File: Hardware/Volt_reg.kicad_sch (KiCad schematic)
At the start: 0 parts

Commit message: USB-C + Voltage stuff
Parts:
- added C28, C29, C30, C33: 0.1uF, Capacitor_SMD:C_0402_1005Metric, symbol Device:C_Small
- added C31: 1uF, Capacitor_SMD:C_0402_1005Metric, symbol Device:C_Small
- added C32: 0.1uF, Capacitor_SMD:C_0603_1608Metric, symbol Device:C_Small
- added D7: P6SMBJ28CA, Diode_SMD:D_SMA, symbol Device:D_TVS_Small_Filled
- added Q2, Q3: BSZ025N04LS, iclr:BSZ025N04LS, symbol iclr:BSZ025N04LS
- added R26: 2m, Resistor_SMD:R_2512_6332Metric_Pad1.40x3.35mm_HandSolder, symbol Device:R
- added R27, R28: 10, Resistor_SMD:R_0402_1005Metric, symbol Device:R_Small
- added R29, R30: 3.3k, Resistor_SMD:R_0402_1005Metric, symbol Device:R_Small
- added R31: 10k, Resistor_SMD:R_0402_1005Metric, symbol Device:R_Small
- added R32: 100k, Resistor_SMD:R_0402_1005Metric, symbol Device:R_Small
- added R33: 5.1k, Resistor_SMD:R_0402_1005Metric, symbol Device:R_Small
- added R34: 4.22k, Resistor_SMD:R_0402_1005Metric, symbol Device:R_Small
- added TP11, TP12: TestPoint, TestPoint:TestPoint_Pad_D1.0mm, symbol Connector:TestPoint
- added U8: INA219AxDCN, Package_TO_SOT_SMD:SOT-23-8, symbol Sensor_Energy:INA219AxDCN
- added U9: LM74810, iclr:SON50P300X300X80-13N-D, symbol iclr:LM74810QDRRRQ1
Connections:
- new net: R33.1, R34.2, U9.5 (OV)
- new net: R32.1, U9.4 (SW)
- new net +3V3: C29.1, R29.1, R30.1, U8.4 (VS)
- new net BUS_VMON: R32.2, R33.2
- new net C: C31.1, C32.1, Q2.5 (D), Q2.6 (D), Q2.7 (D), Q2.8 (D), Q2.A5 (D), Q3.5 (D), Q3.6 (D), Q3.7 (D), Q3.8 (D), Q3.A5 (D), U9.10 (VS), U9.12 (C)
- new net CAP: C31.2, U9.11 (CAP)
- new net DGate: Q2.4 (G), U9.1 (DGATE)
- new net DeployV_Post_Diode: R26.1, R27.1
- new net EN: R31.1, U9.6 (EN/UVLO)
- new net GND: C29.2, C30.2, C32.2, C33.2, D7.2 (A2), R31.2, R34.1, U8.3 (GND), U8.7 (A0), U8.8 (A1), U9.7 (GND)
- new net HGate: Q3.4 (G), U9.8 (HGATE)
- new net PyroPWR: R26.2, R28.1
- new net SCL: R30.2, TP12.1, U8.5 (SCL)
- new net SDA-CurrentSens: R29.2, TP11.1, U8.6 (SDA)
- new net SHNT_IN+: C28.1, R27.2, U8.1 (IN+)
- new net SHNT_IN-: C28.2, C33.1, Q3.1 (S), Q3.2 (S), Q3.3 (S), Q3.A1 (S), R28.2, U8.2 (IN-), U9.9 (OUT)
- new net VIN: C30.1, D7.1 (A1), Q2.1 (S), Q2.2 (S), Q2.3 (S), Q2.A1 (S), U9.2 (A), U9.3 (VSNS)
- no-connect marks 0 -> 1
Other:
- note added: "Add 8A buck-boost converter, takes VIN outputs into High side switch. 8A: https://www.ti.com/lit/ds/symlink/tps55289.pdf?HQS=dis-mous-null-mousermode-dsf-pf-null-wwe&ts=1738081315650&ref_url=https%253A%252F%252Fwww.mouser.com%252F 16A: https://www.ti.com/lit/ds/slvsf01b/slvsf01b.pdf?ts=1734821027897&ref_url=https%253A%252F%252Fwww.google.com%252Furl%253Fq%253Dhttps%253A%252F%252Fwww.ti.com%252Fli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"
- note added: "Batt Mon - 3.0V out @ 35V in Overvoltage cutoff - 32V Check sizing script"

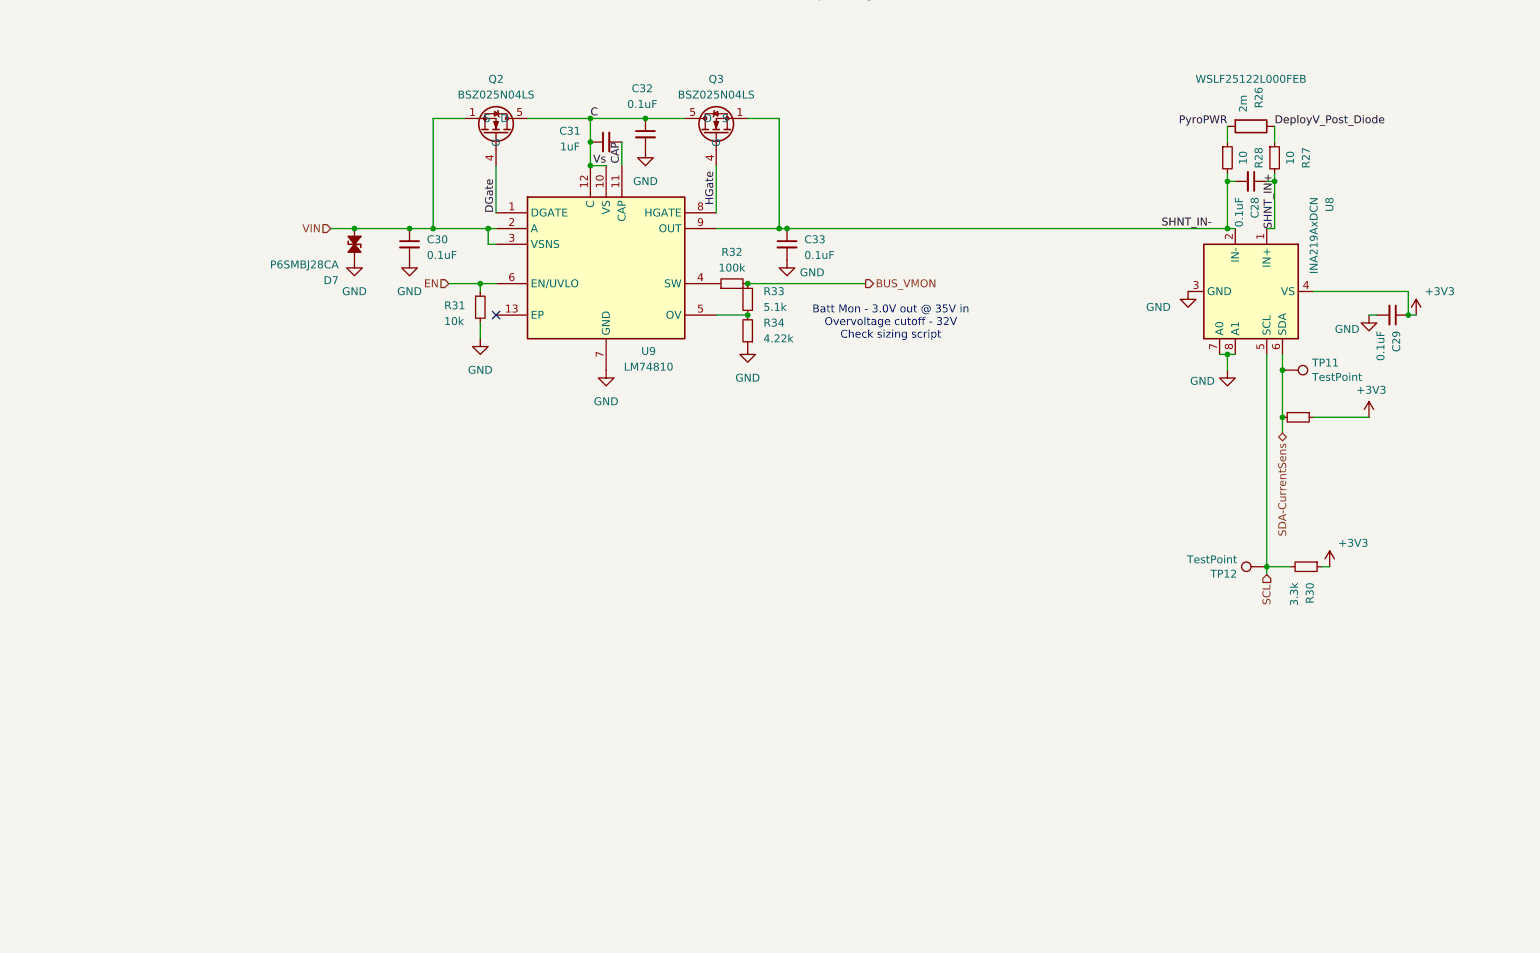
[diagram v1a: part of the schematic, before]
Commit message: Voltage regulation done + used photo ic sensor library
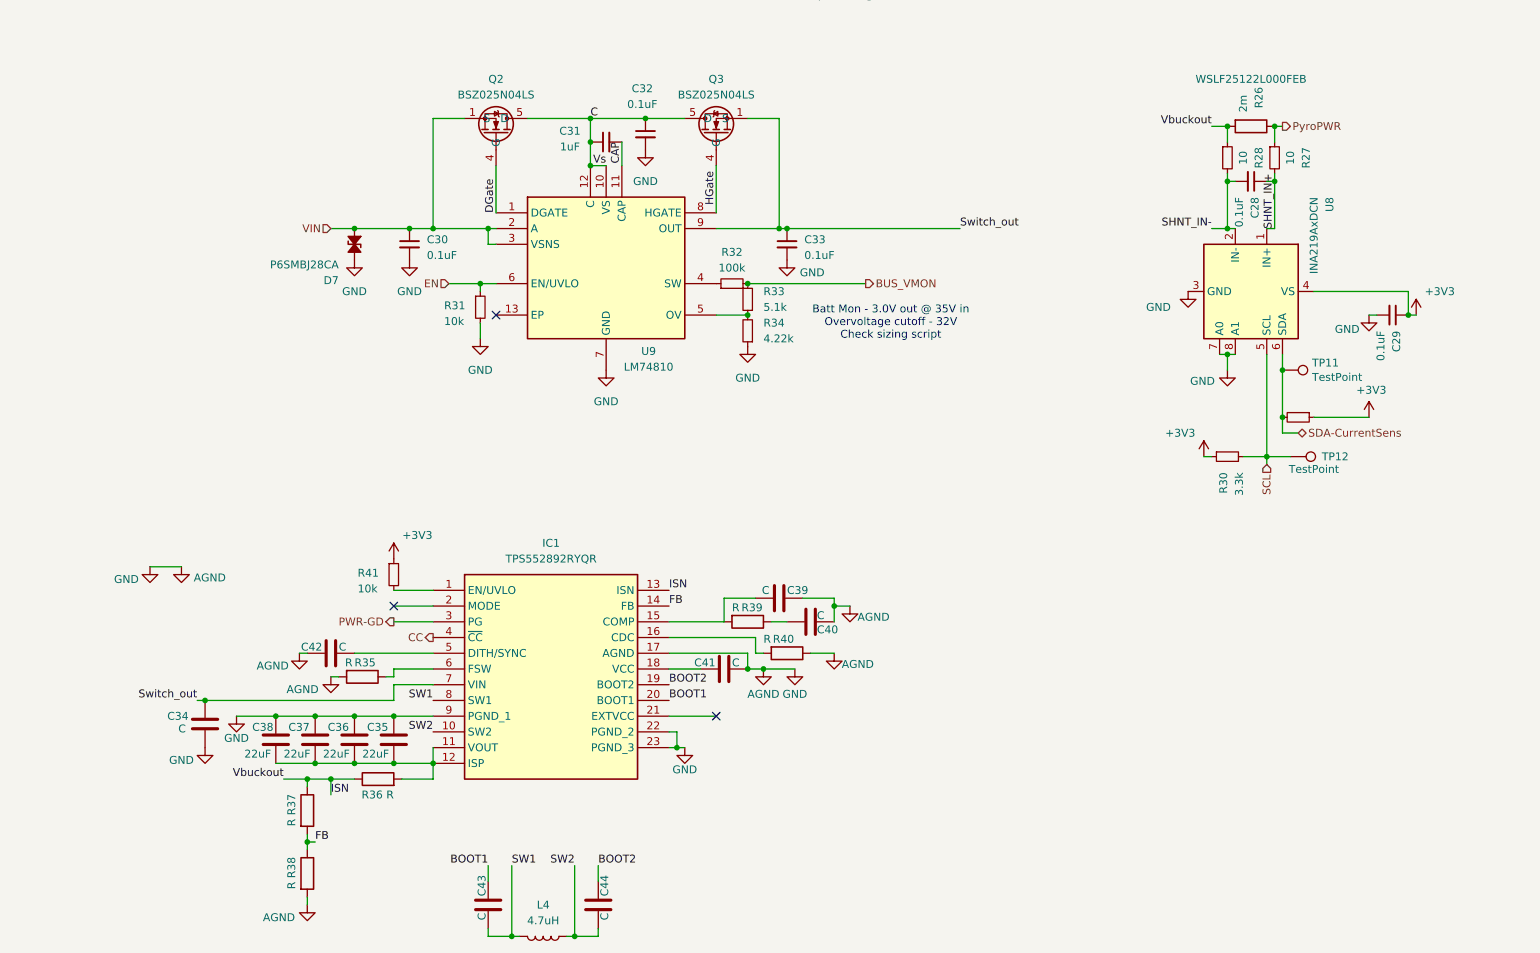
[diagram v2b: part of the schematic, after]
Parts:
- added C34, C39, C40, C41, C42, C43, C44: C, symbol Device:C
- added C35, C36, C37, C38: 22uF, symbol Device:C
- added IC1: TPS552892RYQR, TPS552892RYQR, symbol iclr:TPS552892RYQR
- added L4: 4.7uH, symbol Device:L
- added R35, R36, R37, R38, R39, R40: R, symbol Device:R
- added R41: 10k, Resistor_SMD:R_0402_1005Metric, symbol Device:R_Small
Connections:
- net DeployV_Post_Diode is gone; now on net PyroPWR: R26.1, R27.1
- net +3V3: now also R41.1
- net PyroPWR: no longer R26.2, R28.1
- net SHNT_IN-: no longer C33.1, Q3.1 (S), Q3.2 (S), Q3.3 (S), Q3.A1 (S), U9.9 (OUT)
- net GND renamed AGND
- net AGND: now also C34.2, C35.1, C36.1, C37.1, C38.1, C39.1, C40.1, C41.1, C42.2, IC1.17 (AGND), IC1.22 (PGND_2), IC1.23 (PGND_3), IC1.9 (PGND_1), R35.2, R38.2, R40.1
- new net: IC1.6 (FSW), R35.1
- new net: C42.1, IC1.5 (DITH/SYNC)
- new net: C35.2, C36.2, C37.2, C38.2, IC1.11 (VOUT), IC1.12 (ISP), R36.2
- new net: IC1.16 (CDC), R40.2
- new net: C40.2, R39.1
- new net: C39.2, IC1.15 (COMP), R39.2
- new net: IC1.1 (EN/UVLO), R41.2
- new net: C41.2, IC1.18 (VCC)
- new net BOOT1: C43.2, IC1.20 (BOOT1)
- new net BOOT2: C44.2, IC1.19 (BOOT2)
- new net CC: IC1.4 (~{CC})
- new net FB: IC1.14 (FB), R37.2, R38.1
- new net ISN: IC1.13 (ISN), R26.2, R28.1, R36.1, R37.1
- new net PWR-GD: IC1.3 (PG)
- new net SW1: C43.1, IC1.8 (SW1), L4.2
- new net SW2: C44.1, IC1.10 (SW2), L4.1
- new net Switch_out: C33.1, C34.1, IC1.7 (VIN), Q3.1 (S), Q3.2 (S), Q3.3 (S), Q3.A1 (S), U9.9 (OUT)
- no-connect marks 1 -> 3

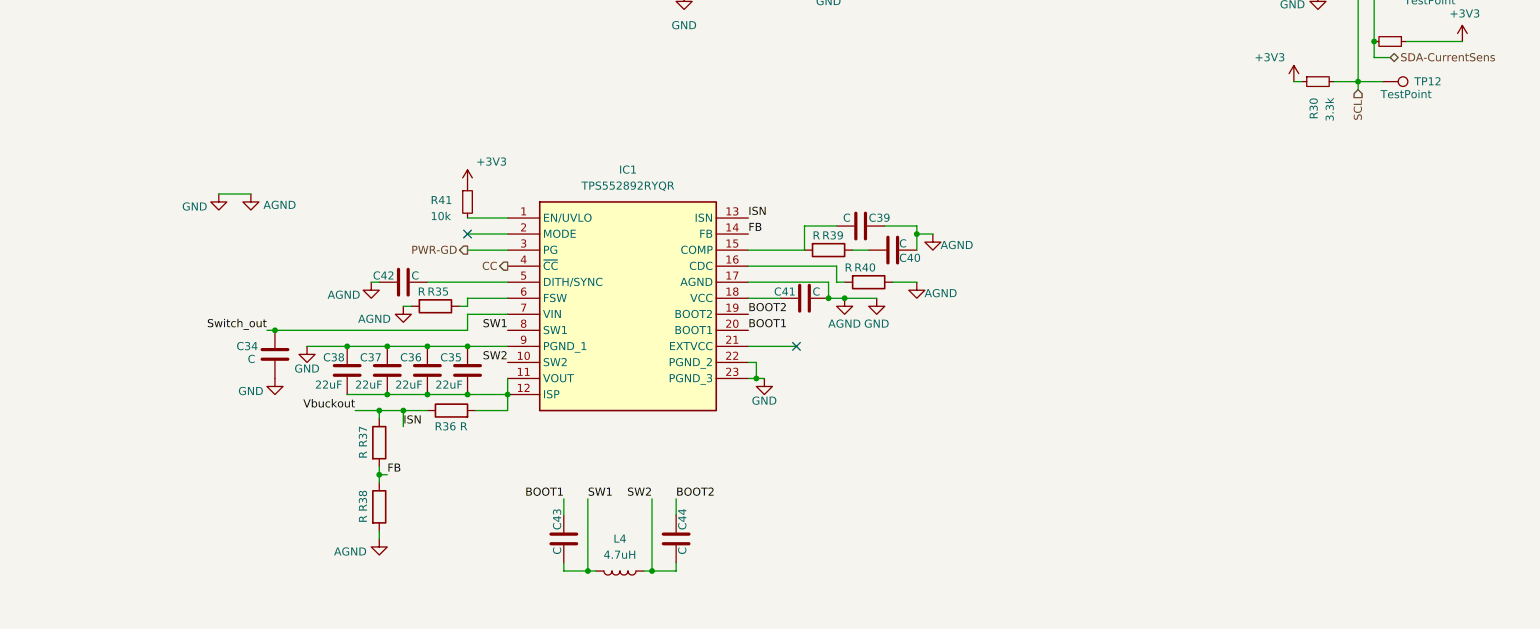
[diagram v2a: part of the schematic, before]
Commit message: New Buck boost converter
+ new sorted circuit, voltage regulation not finalised
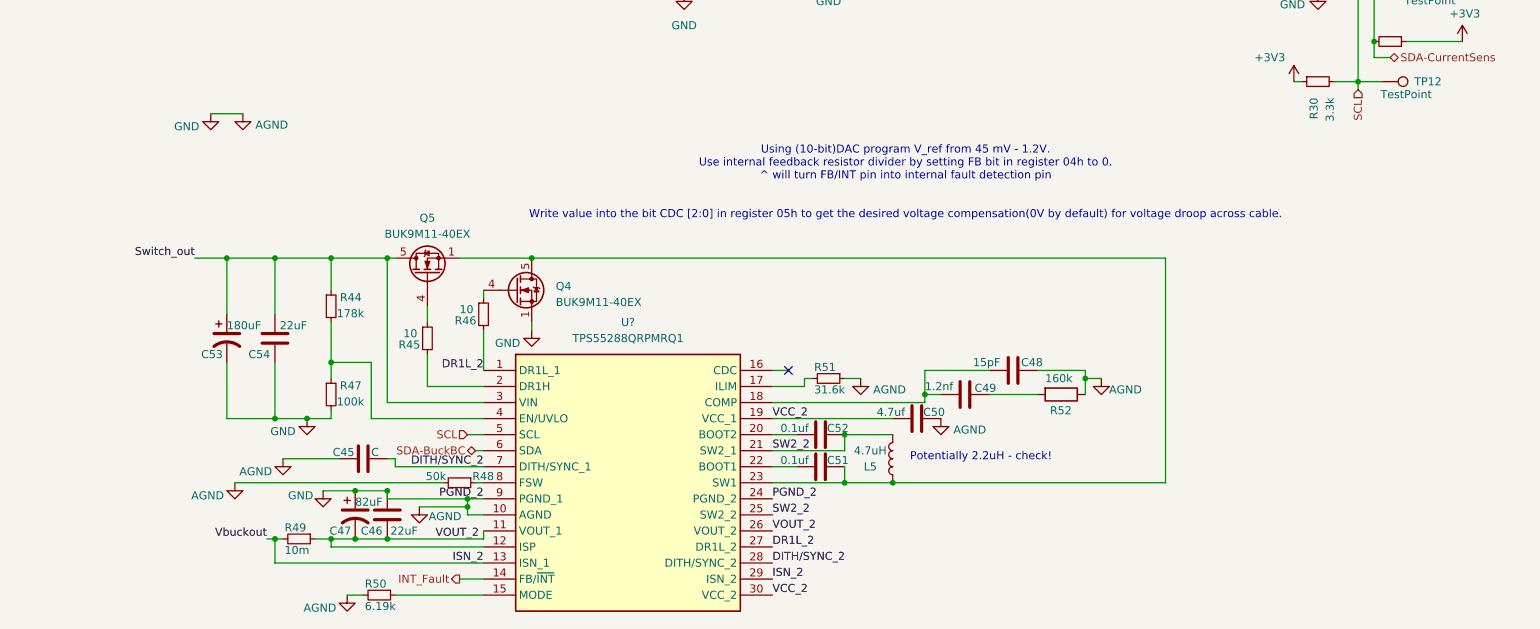
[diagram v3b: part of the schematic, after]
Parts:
- removed C34, C39, C40, C41, C42, C43, C44: C, symbol Device:C
- removed C35, C36, C37, C38: 22uF, symbol Device:C
- removed IC1: TPS552892RYQR, TPS552892RYQR, symbol iclr:TPS552892RYQR
- removed L4: 4.7uH, symbol Device:L
- removed R35, R36, R37, R38, R39, R40: R, symbol Device:R
- removed R41: 10k, Resistor_SMD:R_0402_1005Metric, symbol Device:R_Small
- added C45: C, symbol Device:C
- added C46, C54: 22uF, symbol Device:C
- added C47: 82uF, symbol Device:C_Polarized_US
- added C48: 15pF, symbol Device:C
- added C49: 1.2nf, symbol Device:C
- added C50: 4.7uf, symbol Device:C
- added C51, C52: 0.1uf, symbol Device:C
- added C53: 180uF, symbol Device:C_Polarized_US
- added L5: 4.7uH, symbol Device:L
- added Q4, Q5: BUK9M11-40EX, Package_TO_SOT_SMD:LFPAK33, symbol Transistor_FET:BUK9M11-40EX
- added R44: 178k, Resistor_SMD:R_0402_1005Metric, symbol Device:R_Small
- added R45, R46: 10, Resistor_SMD:R_0402_1005Metric, symbol Device:R_Small
- added R47: 100k, Resistor_SMD:R_0402_1005Metric, symbol Device:R_Small
- added R48: 50k, Resistor_SMD:R_0402_1005Metric, symbol Device:R_Small
- added R49: 10m, Resistor_SMD:R_0402_1005Metric, symbol Device:R_Small
- added R50: 6.19k, Resistor_SMD:R_0402_1005Metric, symbol Device:R_Small
- added R51: 31.6k, Resistor_SMD:R_0402_1005Metric, symbol Device:R_Small
- added R52: 160k, symbol Device:R
- added U?: TPS55288QRPMRQ1, TPS552882QRPMRQ1, symbol iclr:TPS55288QRPMRQ1
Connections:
- net AGND: now also C45.2, C46.2, C47.1, C48.1, C50.1, C53.2, C54.1, Q4.1 (S), Q4.2 (S), Q4.3 (S), R47.2, R48.2, R50.2, R51.1, R52.1, U?.10 (AGND), U?.24 (PGND_2), U?.9 (PGND_1)
- net SCL: now also U?.5 (SCL)
- net Switch_out: now also C53.1, C54.2, Q5.5 (D), R44.1, U?.3 (VIN)
- net ISN renamed ISN_2
- net ISN_2: now also R49.2, U?.13 (ISN_1), U?.29 (ISN_2)
- new net: C51.1, L5.1, Q4.5 (D), Q5.1 (S), Q5.2 (S), Q5.3 (S), U?.23 (SW1)
- new net: C51.2, U?.22 (BOOT1)
- new net: Q4.4 (G), R46.1
- new net: Q5.4 (G), R45.1
- new net: R45.2, U?.2 (DR1H)
- new net: C48.2, C49.2, U?.18 (COMP)
- new net: C49.1, R52.2
- new net: C52.2, U?.20 (BOOT2)
- new net: R44.2, R47.1, U?.4 (EN/UVLO)
- new net: R48.1, U?.8 (FSW)
- new net: R50.1, U?.15 (MODE)
- new net: R51.2, U?.17 (ILIM)
- new net DITH/SYNC_2: C45.1, U?.28 (DITH/SYNC_2), U?.7 (DITH/SYNC_1)
- new net DR1L_2: R46.2, U?.1 (DR1L_1), U?.27 (DR1L_2)
- new net INT_Fault: U?.14 (FB/~{INT})
- new net SDA-BuckBC: U?.6 (SDA)
- new net SW2_2: C52.1, L5.2, U?.21 (SW2_1), U?.25 (SW2_2)
- new net VCC_2: C50.2, U?.19 (VCC_1), U?.30 (VCC_2)
- new net VOUT_2: C46.1, C47.2, R49.1, U?.11 (VOUT_1), U?.12 (ISP), U?.26 (VOUT_2)
- no-connect marks 3 -> 2
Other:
- note added: "Potentially 2.2uH - check!"
- note added: "Using (10-bit)DAC program V_ref from 45 mV - 1.2V. Use internal feedback resistor divider by setting FB bit in register 04h to 0. ^ will turn FB/INT pin into internal fault detection pin Write value into the bit CDC [2:0] in register 05h to get the desired voltage compensation(0V by default) for voltage droop across cable."
